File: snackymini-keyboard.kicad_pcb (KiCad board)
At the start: 2 copper layers, 247.1 x 81.9 mm, 91 parts, among them SW1 SW_PUSH, SW10 SW_PUSH, SW11 SW_PUSH, SW12 SW_PUSH, SW13 SW_PUSH, SW14 SW_PUSH, SW15 SW_PUSH, SW16 SW_PUSH, SW17 SW_PUSH, SW18 SW_PUSH, SW19 SW_PUSH, SW2 SW_PUSH, SW20 SW_PUSH, SW21 SW_PUSH, SW22 SW_PUSH, SW23 SW_PUSH, SW24 SW_PUSH, SW25 SW_PUSH, SW26 SW_PUSH, SW27 SW_PUSH, SW28 SW_PUSH, SW29 SW_PUSH, SW3 SW_PUSH, SW30 SW_PUSH, SW31 SW_PUSH, SW32 SW_PUSH, SW33 SW_PUSH, SW34 SW_PUSH, SW35 SW_PUSH, SW36 SW_PUSH, SW37 SW_PUSH, SW38 SW_PUSH, SW39 SW_PUSH, SW4 SW_PUSH, SW40 SW_PUSH, SW41 SW_PUSH, SW42 SW_PUSH, SW43 SW_PUSH, SW44 SW_PUSH, SW45 SW_PUSH, SW5 SW_PUSH, SW6 SW_PUSH, SW7 SW_PUSH, SW8 SW_PUSH, SW9 SW_PUSH, U1 Teensy3.2

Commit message: Update layout and routing, add corner mount hole
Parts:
- moved D41 125.8 mm to (235.5, 118.2)
- moved U1 77.8 mm to (99.7, 61.3)
- moved D1 61.8 mm to (99.9, 61.1), turned to 90 degrees
- moved D2 61.5 mm to (119.0, 61.7), turned to 90 degrees
- moved D12 56.7 mm to (307.1, 72.4)
- moved D24 56.7 mm to (309.5, 91.3)
- moved D36 56.7 mm to (313.9, 110.2)
- moved D43 56.7 mm to (276.2, 129.4)
- moved SW23 56.7 mm to (285.2, 81.9)
- moved D39 56.7 mm to (145.3, 129.4)
- moved D22 56.7 mm to (266.3, 91.6)
- moved SW14 56.7 mm to (114.0, 81.9)
- moved D15 56.7 mm to (133.2, 91.3)
- moved D28 56.7 mm to (162.3, 110.2)
- moved D38 56.7 mm to (119.1, 129.0)
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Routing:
- net COL12: track 90.1 -> 251.4 mm
- net COL4: track 174.2 -> 51.2 mm, vias 1 -> 0
- net COL1: track 188.0 -> 66.6 mm
- net COL9: track 69.2 -> 173.5 mm
- net COL6: track 76.3 -> 156.8 mm, vias 0 -> 1
- net COL10: track 236.4 -> 298.8 mm
- net COL3: track 138.8 -> 200.3 mm
- net COL11: track 117.9 -> 170.2 mm
- net Net-(D41-Pad2): track 61.5 -> 19.5 mm
- net COL5: track 131.5 -> 98.4 mm
- net ROW1: track 416.1 -> 445.7 mm
- net COL7: track 242.4 -> 267.0 mm
- net ROW2: track 440.5 -> 425.7 mm
- net ROW3: track 414.4 -> 424.8 mm, vias 0 -> 1
- net COL2: track 128.3 -> 119.8 mm
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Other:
- board size 247.1 x 81.9 mm -> 257.8 x 192.7 mm

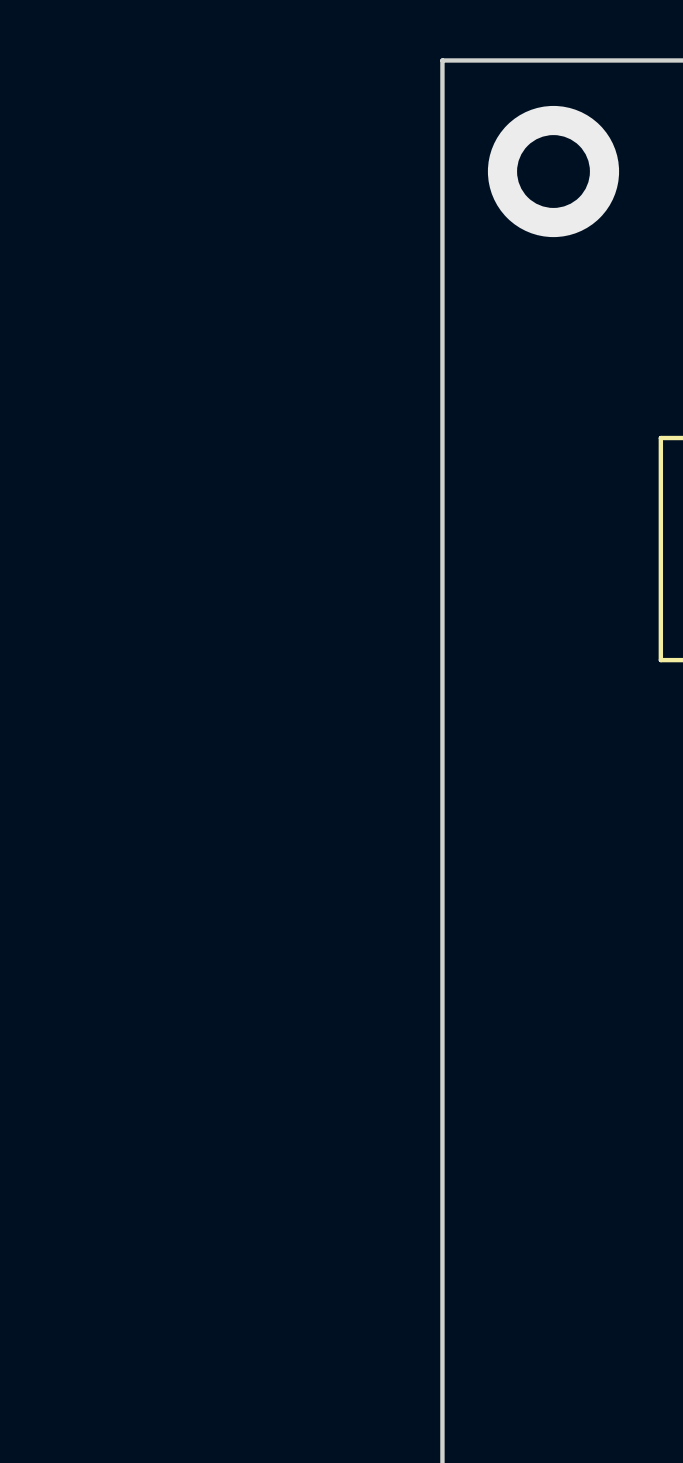
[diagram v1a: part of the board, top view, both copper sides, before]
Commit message: Update PCB pinout
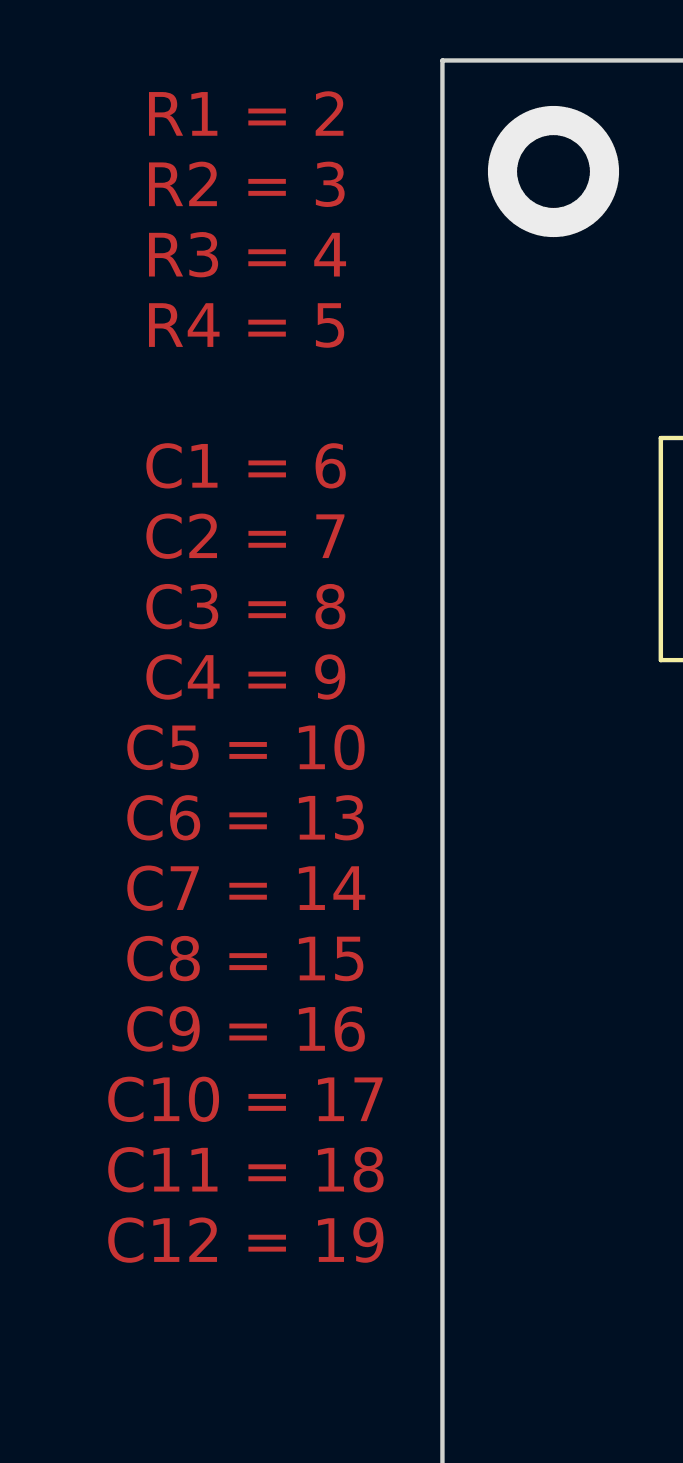
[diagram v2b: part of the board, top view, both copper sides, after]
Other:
- board text added: "R1 = 2 R2 = 3 R3 = 4 R4 = 5 C1 = 6 C2 = 7 C3 = 8 C4 = 9 C5 = 10 C6 = 13 C7 = 14 C8 = 15 C9 = 16 C10 = 17 C11 = 18 C12 = 19"
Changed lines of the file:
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@@
   (general
     (thickness 1.6)
-    (drawings 671)
+    (drawings 672)
     (tracks 474)
     (zones 0)
@@
     (pad HOLE np_thru_hole circle (at 5.08 0) (size 1.7018 1.7018) (drill 1.7018) (layers *.Cu))
   )
+  (gr_text "R1 = 2\nR2 = 3\nR3 = 4\nR4 = 5\n\nC1 = 6\nC2 = 7\nC3 = 8\nC4 = 9\nC5 = 10\nC6 = 13\nC7 = 14\nC8 = 15\nC9 = 16\nC10 = 17\nC11 = 18\nC12 = 19" (at 66.421 65.786) (layer F.Cu)
+    (effects (font (size 1.5 1.5) (thickness 0.3)))
+  )
   (gr_line (start 330.962 143.256) (end 73.152 143.256) (layer Edge.Cuts) (width 0.15))
